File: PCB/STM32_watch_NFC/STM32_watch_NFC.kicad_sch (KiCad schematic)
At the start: 36 parts, among them J1 Conn_01x06_Socket, Q1 2N7000, SW1 SW_DPST_x2, SW2 SW_DPST_x2, SW3 SW_DPST_x2, U1 STM32L031G6Ux, U3 TM1637, Y2 32.768kHz

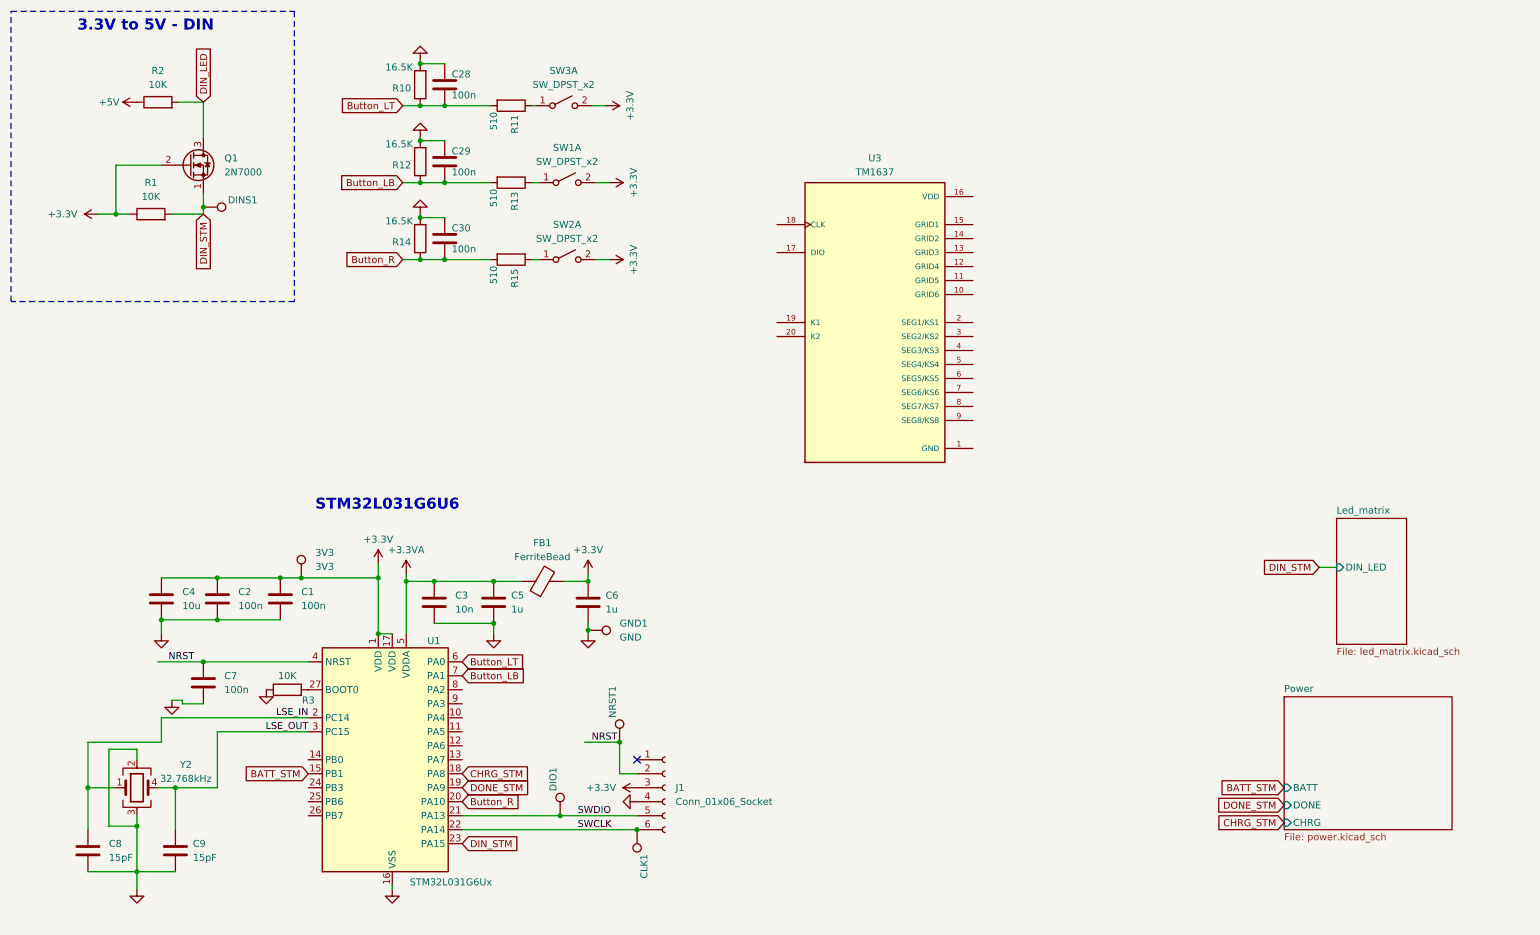
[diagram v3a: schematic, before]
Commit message: Kicad - new Routing 4.5
NEW 7-segment display + connection, new charger, charging status
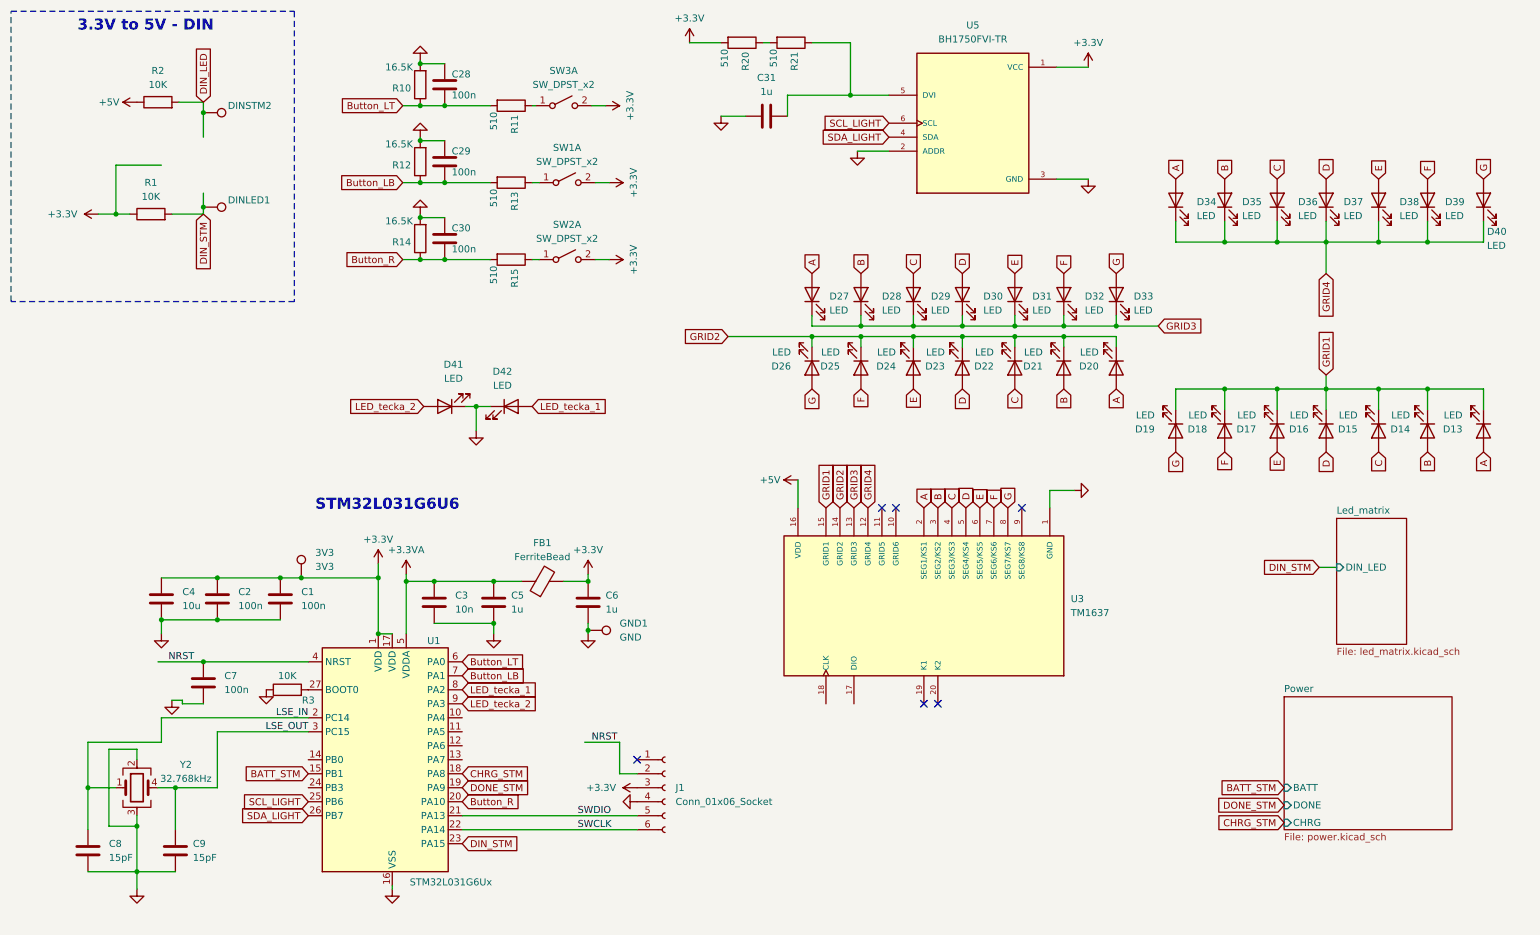
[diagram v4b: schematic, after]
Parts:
- removed CLK1, DIO1, NRST1: ~, TestPoint:TestPoint_Pad_D1.0mm, symbol Connector:TestPoint
- removed Q1: 2N7000, Package_TO_SOT_SMD:TSOT-23, symbol Transistor_FET:2N7000
- added C31: 1u, Capacitor_SMD:C_0402_1005Metric, symbol Device:C
- added D13, D14, D15, D16, D17, D18, D19, D20, D21, D22, D23, D24, D25, D26, D27, D28, D29, D30, D31, D32, D33, D34, D35, D36, D37, D38, D39, D40, D41, D42: LED, LED_SMD:LED_0402_1005Metric, symbol Device:LED
- added DINSTM2: ~, TestPoint:TestPoint_Pad_D1.0mm, symbol Connector:TestPoint
- added R20, R21: 510, Resistor_SMD:R_0402_1005Metric, symbol Device:R
- added U5: BH1750FVI-TR, BH1750FVI-TR:XDCR_BH1750FVI-TR, symbol BH1750FVI-TR:BH1750FVI-TR
- renumbered DINS1 to DINLED1
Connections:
- net +3.3V: now also R20.2, U5.1 (VCC)
- net +5V: now also U3.16 (VDD)
- net DIN_LED: now also DINSTM2.1
- net GND: now also U3.1 (GND), C31.2, D41.1 (K), D42.1 (K), U5.2 (ADDR), U5.3 (GND)
- net SCL_LIGHT: now reaches U1.25 (PB6)
- net SCL_LIGHT: now also U5.6 (SCL)
- net SDA_LIGHT: now reaches U1.26 (PB7)
- net SDA_LIGHT: now also U5.4 (SDA)
- net LED_tecka_1: now reaches U1.8 (PA2)
- net LED_tecka_1: now also D42.2 (A)
- net LED_tecka_2: now reaches U1.9 (PA3)
- net LED_tecka_2: now also D41.2 (A)
- net GRID4: now reaches U3.12 (GRID4)
- net GRID4: now also D34.1 (K), D35.1 (K), D36.1 (K), D37.1 (K), D38.1 (K), D39.1 (K), D40.1 (K)
- net GRID3: now reaches U3.13 (GRID3)
- net GRID3: now also D27.1 (K), D28.1 (K), D29.1 (K), D30.1 (K), D31.1 (K), D32.1 (K), D33.1 (K)
- net GRID2: now reaches U3.14 (GRID2)
- net GRID2: now also D20.1 (K), D21.1 (K), D22.1 (K), D23.1 (K), D24.1 (K), D25.1 (K), D26.1 (K)
- net GRID1: now reaches U3.15 (GRID1)
- net GRID1: now also D13.1 (K), D14.1 (K), D15.1 (K), D16.1 (K), D17.1 (K), D18.1 (K), D19.1 (K)
- net A: now reaches U3.2 (SEG1/KS1)
- net A: now also D13.2 (A), D20.2 (A), D27.2 (A), D34.2 (A)
- net B: now reaches U3.3 (SEG2/KS2)
- net B: now also D14.2 (A), D21.2 (A), D28.2 (A), D35.2 (A)
- net C: now reaches U3.4 (SEG3/KS3)
- net C: now also D15.2 (A), D22.2 (A), D29.2 (A), D36.2 (A)
- net D: now reaches U3.5 (SEG4/KS4)
- net D: now also D16.2 (A), D23.2 (A), D30.2 (A), D37.2 (A)
- net E: now reaches U3.6 (SEG5/KS5)
- net E: now also D17.2 (A), D24.2 (A), D31.2 (A), D38.2 (A)
- net F: now reaches U3.7 (SEG6/KS6)
- net F: now also D18.2 (A), D25.2 (A), D32.2 (A), D39.2 (A)
- net G: now reaches U3.8 (SEG7/KS7)
- net G: now also D19.2 (A), D26.2 (A), D33.2 (A), D40.2 (A)
- new net: R20.1, R21.2
- new net: C31.1, R21.1, U5.5 (DVI)
- no-connect marks 1 -> 6
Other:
- moved on the sheet: U3

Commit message: Kicad/STM - new Routing 5
All STM32 peripherals connected, new firmware file + new code in it :)
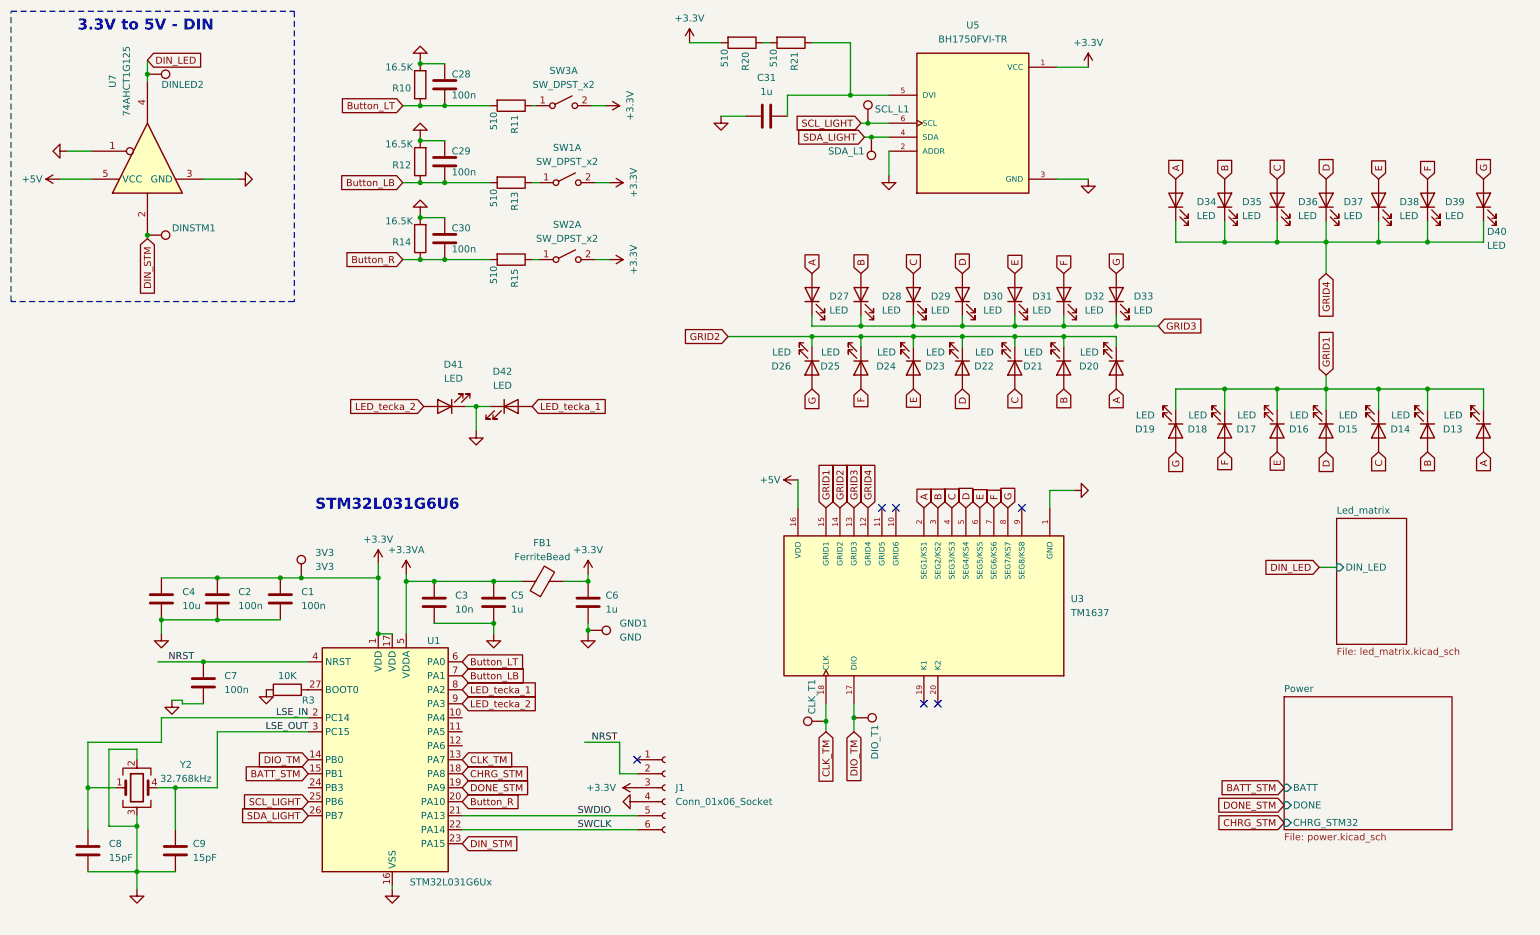
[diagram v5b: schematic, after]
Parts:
- removed R1, R2: 10K, Resistor_SMD:R_0402_1005Metric, symbol Device:R
- added CLK_T1, DIO_T1, SCL_L1, SDA_L1: ~, TestPoint:TestPoint_Pad_D1.0mm, symbol Connector:TestPoint
- added U7: 74AHCT1G125, Package_TO_SOT_SMD:SOT-353_SC-70-5, symbol 74xGxx:74AHCT1G125
- renumbered DINSTM2 to DINLED2, DINLED1 to DINSTM1
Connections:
- net +5V: now also U7.5 (VCC)
- net DIN_LED: now also U7.4
- net DIN_STM: now also U7.2
- net GND: now also U7.1, U7.3 (GND)
- net SCL_LIGHT: now also SCL_L1.1
- net SDA_LIGHT: now also SDA_L1.1
- net CLK_TM: now reaches U1.13 (PA7)
- net CLK_TM: now also U3.18 (CLK), CLK_T1.1
- net DIO_TM: now reaches U1.14 (PB0)
- net DIO_TM: now also U3.17 (DIO), DIO_T1.1
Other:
- sheet Power ports: added CHRG_STM32; removed CHRG
- moved on the sheet: DINLED2, DINSTM1

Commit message: TM1637 - in next commit I will delete the driver and connect the leds directly through matrix
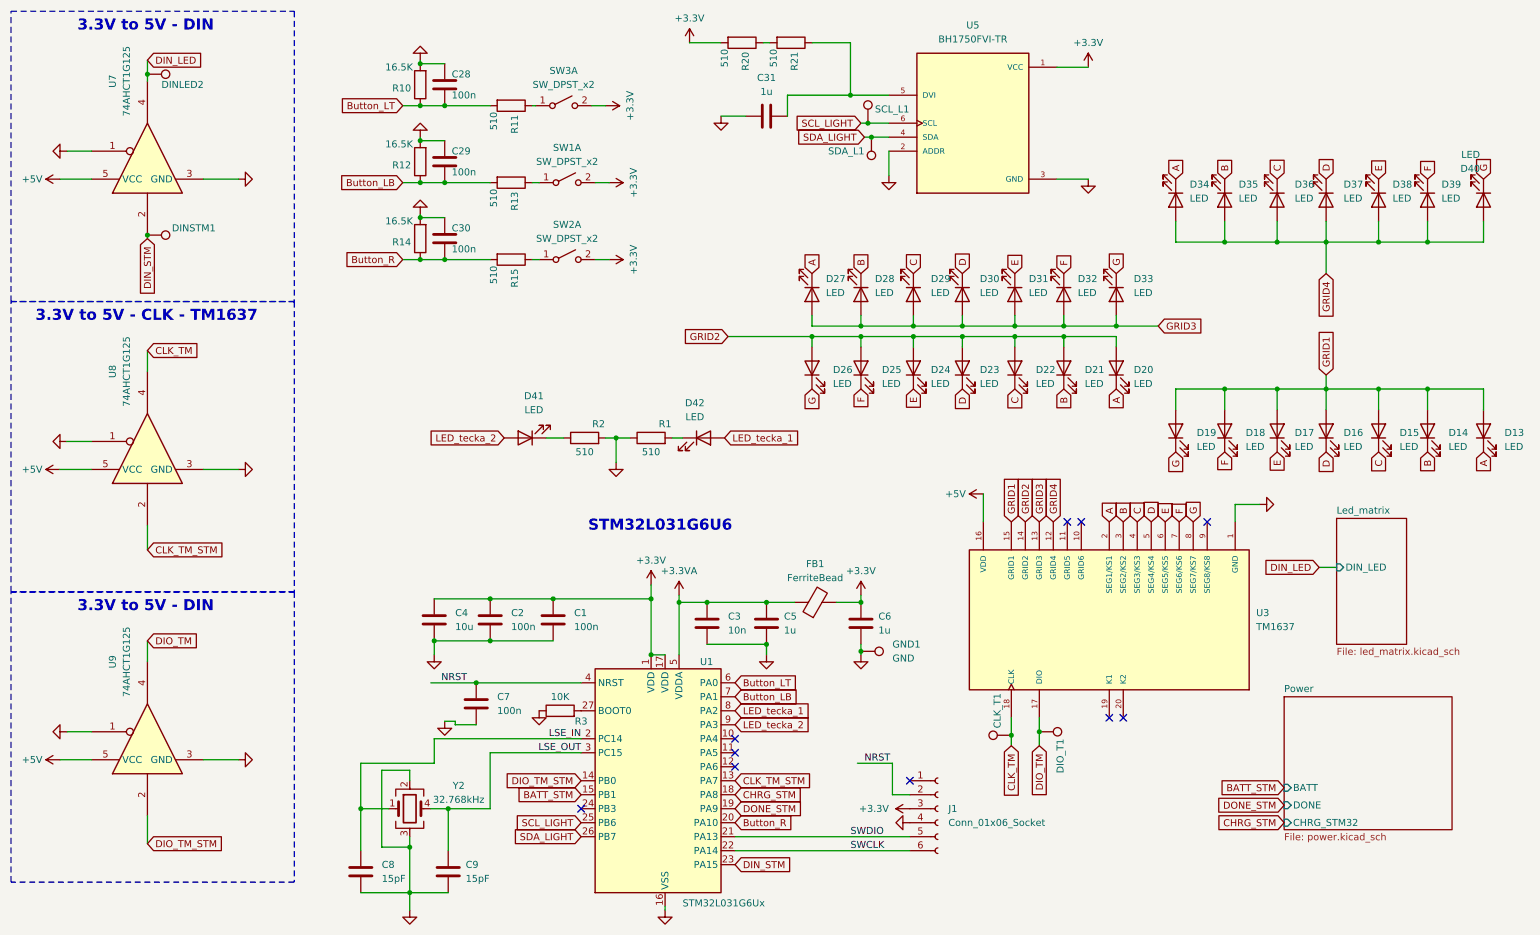
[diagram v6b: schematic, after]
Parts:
- removed 3V3: 3V3, TestPoint:TestPoint_Pad_D1.5mm, symbol Connector:TestPoint
- added R1, R2: 510, Resistor_SMD:R_0402_1005Metric, symbol Device:R
- added U8, U9: 74AHCT1G125, Package_TO_SOT_SMD:SOT-353_SC-70-5, symbol 74xGxx:74AHCT1G125
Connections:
- net +5V: now also U8.5 (VCC), U9.5 (VCC)
- net A: now also D13.1 (K), D20.1 (K), D27.1 (K), D34.1 (K); no longer D13.2 (A), D20.2 (A), D27.2 (A), D34.2 (A)
- net B: now also D14.1 (K), D21.1 (K), D28.1 (K), D35.1 (K); no longer D14.2 (A), D21.2 (A), D28.2 (A), D35.2 (A)
- net C: now also D15.1 (K), D22.1 (K), D29.1 (K), D36.1 (K); no longer D15.2 (A), D22.2 (A), D29.2 (A), D36.2 (A)
- net CLK_TM: now also U8.4; no longer U1.13 (PA7)
- net D: now also D16.1 (K), D23.1 (K), D30.1 (K), D37.1 (K); no longer D16.2 (A), D23.2 (A), D30.2 (A), D37.2 (A)
- net DIO_TM: now also U9.4; no longer U1.14 (PB0)
- net E: now also D17.1 (K), D24.1 (K), D31.1 (K), D38.1 (K); no longer D17.2 (A), D24.2 (A), D31.2 (A), D38.2 (A)
- net F: now also D18.1 (K), D25.1 (K), D32.1 (K), D39.1 (K); no longer D18.2 (A), D25.2 (A), D32.2 (A), D39.2 (A)
- net G: now also D19.1 (K), D26.1 (K), D33.1 (K), D40.1 (K); no longer D19.2 (A), D26.2 (A), D33.2 (A), D40.2 (A)
- net GND: now also R1.1, R2.2, U8.1, U8.3 (GND), U9.1, U9.3 (GND); no longer D41.1 (K), D42.1 (K)
- net GRID1: now also D13.2 (A), D14.2 (A), D15.2 (A), D16.2 (A), D17.2 (A), D18.2 (A), D19.2 (A); no longer D13.1 (K), D14.1 (K), D15.1 (K), D16.1 (K), D17.1 (K), D18.1 (K), D19.1 (K)
- net GRID2: now also D20.2 (A), D21.2 (A), D22.2 (A), D23.2 (A), D24.2 (A), D25.2 (A), D26.2 (A); no longer D20.1 (K), D21.1 (K), D22.1 (K), D23.1 (K), D24.1 (K), D25.1 (K), D26.1 (K)
- net GRID3: now also D27.2 (A), D28.2 (A), D29.2 (A), D30.2 (A), D31.2 (A), D32.2 (A), D33.2 (A); no longer D27.1 (K), D28.1 (K), D29.1 (K), D30.1 (K), D31.1 (K), D32.1 (K), D33.1 (K)
- net GRID4: now also D34.2 (A), D35.2 (A), D36.2 (A), D37.2 (A), D38.2 (A), D39.2 (A), D40.2 (A); no longer D34.1 (K), D35.1 (K), D36.1 (K), D37.1 (K), D38.1 (K), D39.1 (K), D40.1 (K)
- new net: D42.1 (K), R1.2
- new net: D41.1 (K), R2.1
- new net CLK_TM_STM: U1.13 (PA7), U8.2
- new net DIO_TM_STM: U1.14 (PB0), U9.2
- no-connect marks 6 -> 10
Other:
- note added: "3.3V to 5V - CLK - TM1637"
- moved on the sheet: C1, C2, C3, C4, C5, C6, C7, C8, C9, CLK_T1, D13, D14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
